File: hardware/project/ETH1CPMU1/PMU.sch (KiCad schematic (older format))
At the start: 0 parts

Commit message: Schematic design
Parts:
- added C1401: C, symbol Device:C
- added C1402: 100p, symbol Device:C
- added C1403: 1n, symbol Device:C
- added C1404: 3n3, symbol Device:C
- added C1405, C1406: 10p, symbol Device:C
- added C1407, C1409, C1411: 100n, symbol Device:C
- added C1408, C1410, C1412: 10u, symbol Device:C
- added K1401, K1402, K? (x12): HE3621A0510, symbol ETH1CPMU1:HE3621A0510
- added Q1401, Q1402: BC847, Package_TO_SOT_SMD:SOT-23, symbol Transistor_BJT:BC847
- added R1401: 5k1, symbol Device:R
- added R1402: 124k, symbol Device:R
- added R1403: 12k4, symbol Device:R
- added R1404: 1k24, symbol Device:R
- added R1405: 124, symbol Device:R
- added R1406: 12R4, symbol Device:R
- added R1407, R1408: R, symbol Device:R
- added R1410, R1411: 10k, symbol Device:R
- added U1401: AD5520, symbol ETH1CPMU1:AD5520
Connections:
- new net: K?.1, U1401.30 (GUARD)
- new net: K?.1, U1401.34 (MEASVL)
- new net: C1401.1, R1402.1, U1401.38 (MEASIOH), U1401.39 (FOH0)
- new net: R1403.1, U1401.40 (MEASI1H), U1401.41 (FOH1)
- new net: R1404.1, U1401.42 (MEASI2H), U1401.43 (FOH2)
- new net: R1405.1, U1401.44 (MEASI3H), U1401.45 (FOH3)
- new net: K1401.4, R1406.1, U1401.46 (MEASI4H)
- new net: K1402.4, R1407.1, R1408.1, U1401.47 (MEASI5H)
- new net: C1404.2, U1401.51 (COMPOUT0)
- new net: C1403.2, U1401.52 (COMPOUT1)
- new net: C1402.2, U1401.53 (COMPOUT2)
- new net: C1404.1, U1401.54 (COMPIN0)
- new net: C1403.1, U1401.55 (COMPIN1)
- new net: C1402.1, U1401.56 (COMPIN2)
- new net: K1401.1, K1402.1
- new net: K1401.3, Q1401.3 (C)
- new net: K1402.3, Q1402.3 (C)
- new net: C1406.1, Q1402.1 (B), R1411.2
- new net: C1405.1, Q1401.1 (B), R1410.2
- new net +15VF: C1411.1, C1412.1, U1401.27 (AVCC), U1401.33 (AVCCG), U1401.50 (AVCCB)
- new net +3.3VF: C1407.1, C1408.1, U1401.18 (DVDD), U1401.3 (DVDD)
- new net +5VF: K1401.2, K1402.2
- new net -15VF: C1409.1, C1410.1, U1401.26 (AVEE), U1401.29 (AVEEG), U1401.48 (AVEEB)
- new net A: K?.4
- new net AGNDF: C1409.2, C1410.2, C1411.2, C1412.2, K?.1, U1401.2 (CPL), U1401.28 (AGND), U1401.57 (REFGND), U1401.59 (REFGND), U1401.64 (CLL)
- new net B: K?.4
- new net C: K?.4
- new net DGNDF: C1405.2, C1406.2, C1407.2, C1408.2, Q1401.2 (E), Q1402.2 (E), U1401.17 (GDND), U1401.7 (DGND)
- new net E: K?.4
- new net F: K?.4, K?.4
- new net GUARDIN: K?.1, U1401.32 (GUARDIN)
- new net MEASIL: C1401.2, K?.1, R1402.2, R1403.2, R1404.2, R1405.2, R1406.2, R1407.2, R1408.2, U1401.37 (MEASIL)
- new net MEASVH: K?.1, U1401.36 (MEASHV)
- new net PMU_AC0: U1401.15 (AC0)
- new net PMU_AC1: U1401.16 (AC1)
- new net PMU_AM0: U1401.21 (AM0)
- new net PMU_AM1: U1401.20 (AM1)
- new net PMU_AM2: U1401.19 (AM2)
- new net PMU_CLHDETECT: U1401.8 (CLHDETECT)
- new net PMU_CLLDETECT: U1401.9 (CLLDETECT)
- new net PMU_CPCK: U1401.6 (CPCK)
- new net PMU_CPOH: U1401.4 (CPOH)
- new net PMU_CPOL: U1401.5 (CPOL)
- new net PMU_MSEL: U1401.24 (MSEL)
- new net PMU_QM4: R1411.1, U1401.10 (QM4)
- new net PMU_QM5: R1410.1, U1401.11 (QM5)
- new net PMU_STANDBY: U1401.22 (STANDBY)
- new net PMU_~CS: U1401.13 (~CS), U1401.25 (CPSEL)
- new net PMU_~MOE: U1401.12 (~MOE), U1401.23 (FSEL)
- new net PMU_~STB: U1401.14 (~STB)

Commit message: Schematic design
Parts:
- removed K? (x12): HE3621A0510, symbol ETH1CPMU1:HE3621A0510
- added C1303, C1304, C1305: 100n, symbol Device:C
- added C1413, C1414, C1415, C1416, C1417, C1418: 10p, symbol Device:C
- added K1403, K1404, K1405, K1406, K1407, K1408: HE3621A0510, symbol ETH1CPMU1:HE3621A0510
- added Q1403, Q1404, Q1405, Q1406, Q1407, Q1408: BC847, Package_TO_SOT_SMD:SOT-23, symbol Transistor_BJT:BC847
- added R1409: 5k1, symbol Device:R
- added R1412, R1413, R1414, R1415, R1416, R1417: 10k, symbol Device:R
- added U1402: AD8010, symbol ETH1CPMU1:AD8010
- added U1403: DG419LEUA, Package_SO:MSOP-8_3x3mm_P0.65mm, symbol Analog_Switch:DG419LEUA
- R1402: value 124k -> 125k
- R1403: value 12k4 -> 12k5
- R1404: value 1k24 -> 1k25
- R1405: value 124 -> 125
- R1406: value 12R4 -> 12R5
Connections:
- net +15VF: now also C1304.1, U1402.7 (V+), U1403.4 (V+)
- net +3.3VF: now also C1303.1, U1403.5 (VL)
- net +5VF: now also K1403.2, K1404.2, K1405.2, K1406.2, K1407.2, K1408.2
- net -15VF: now also C1305.1, U1402.4 (V-), U1403.7 (V-)
- net A: now also K1404.4
- net AGNDF: now also K1408.1
- net B: now also K1405.4
- net C: now also K1407.4
- net DGNDF: now also C1303.2, C1304.2, C1305.2, C1413.2, C1414.2, C1415.2, C1416.2, C1417.2, C1418.2, Q1403.2 (E), Q1404.2 (E), Q1405.2 (E), Q1406.2 (E), Q1407.2 (E), Q1408.2 (E), U1403.3 (GND)
- net E: now also K1408.4
- net F: now also K1403.4, K1406.4
- net PMU_QM4: now also R1410.1; no longer R1411.1
- net PMU_QM5: now also R1411.1; no longer R1410.1
- net PMU_~CS: no longer U1401.25 (CPSEL)
- net at U1401.30 (GUARD): now also K1407.1
- net at U1401.34 (MEASVL): now also K1405.1
- net at U1401.49 (FOH): now also R1401.2
- net PMU_MEASOUT: now reaches U1401.58 (MEASOUT)
- net PMU_MEASIOUT: now reaches U1401.60 (MEASIOUT)
- net PMU_MEASVOUT: now reaches U1401.61 (MEASVOUT)
- net at U1401.62 (FIN): now also U1403.1
- net at K1401.1, K1402.1: now also R1409.1, U1402.6
- net at R1401.1: now also U1402.3 (+)
- net GUARDIN: no longer names the net of U1401.32 (GUARDIN)
- net GUARDIN: now also K1406.1
- net MEASIL: no longer names the net of C1401.2, R1402.2, R1403.2, R1404.2, R1405.2, R1406.2, R1407.2, R1408.2, U1401.37 (MEASIL)
- net MEASIL: now also K1403.1
- net MEASVH: no longer names the net of U1401.36 (MEASHV)
- net MEASVH: now also K1404.1
- new net: C1413.1, Q1403.1 (B), R1412.2
- new net: K1403.3, Q1403.3 (C)
- new net: C1414.1, Q1404.1 (B), R1413.2
- new net: K1404.3, Q1404.3 (C)
- new net: K1405.3, Q1405.3 (C)
- new net: K1406.3, Q1406.3 (C)
- new net: K1407.3, Q1407.3 (C)
- new net: K1408.3, Q1408.3 (C)
- new net: C1415.1, Q1405.1 (B), R1414.2
- new net: R1409.2, U1402.2 (-)
- new net: C1416.1, Q1406.1 (B), R1415.2
- new net: C1417.1, Q1407.1 (B), R1416.2
- new net: C1418.1, Q1408.1 (B), R1417.2
- new net AC_FOURCE: U1403.8
- new net DC_FOURCE: U1403.2
- new net FOURCE_SELECT: U1403.6
- new net PMU_CPSEL: U1401.25 (CPSEL)
- new net R_GND: R1417.1
- new net R_GUARD: R1416.1
- new net R_GUARDIN: R1415.1
- new net R_MEASHV: R1413.1
- new net R_MEASIL: R1412.1
- new net R_MEASVL: R1414.1
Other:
- note added: "RELAY CONTROL"
- moved on the sheet: C1401, C1402, C1403, C1404, C1405, C1406, C1407, C1408, C1409, C1410, C1411, C1412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

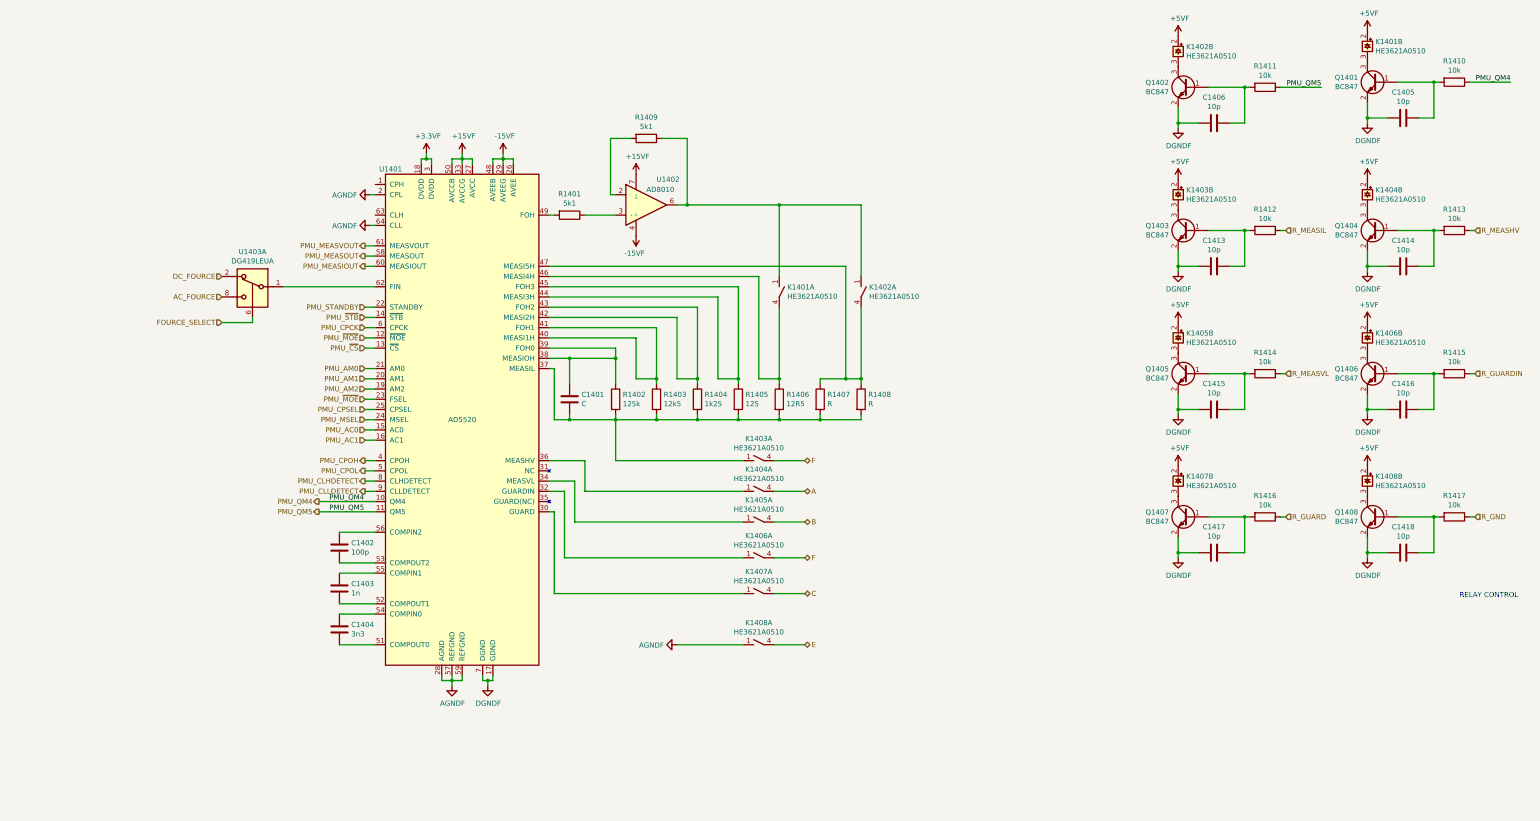
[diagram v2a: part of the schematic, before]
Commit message: Function generator schematic design.
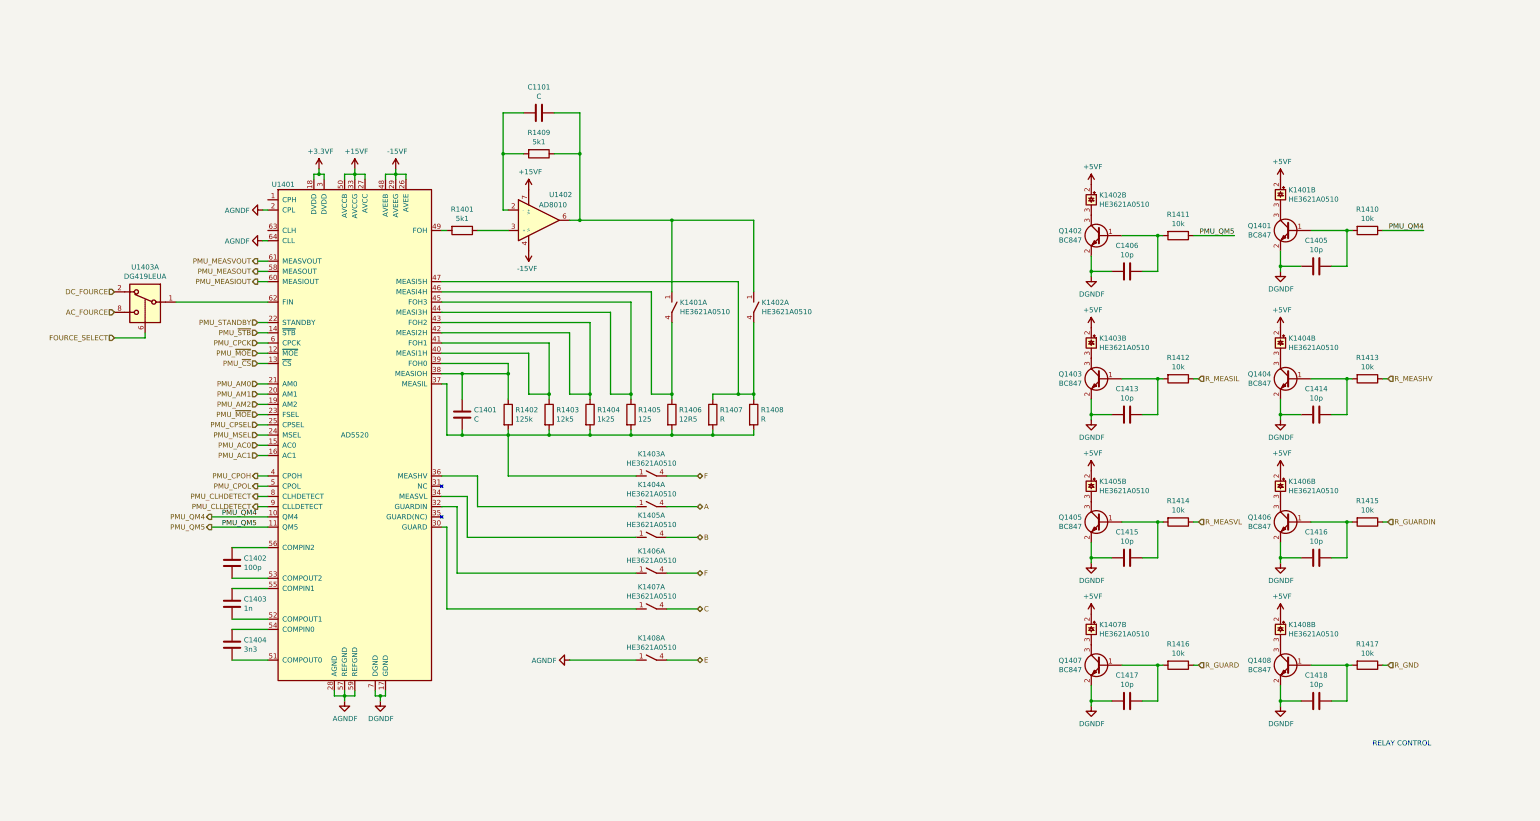
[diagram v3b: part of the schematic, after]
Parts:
- added C1101: C, symbol Device:C
- C1303, C1304, C1305, C1402, C1403, C1404, C1405, C1406, C1407, C1409, C1411, C1413, C1414, C1415, C1416, C1417, C1418: footprint (none) -> Capacitor_SMD:C_0603_1608Metric_Pad1.05x0.95mm_HandSolder
- C1408, C1410, C1412: footprint (none) -> Capacitor_SMD:C_1206_3216Metric_Pad1.42x1.75mm_HandSolder
- R1410, R1411, R1412, R1413, R1414, R1415, R1416, R1417: footprint (none) -> Resistor_SMD:R_0603_1608Metric_Pad1.05x0.95mm_HandSolder
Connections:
- net at R1409.2, U1402.2 (-): now also C1101.2
- net at K1401.1, K1402.1, R1409.1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: now also C1101.1
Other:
- moved on the sheet: C1401, C1402, C1403, C1404, C1405, C1406, C1413, C1414, C1415, C1416, C1417, C1418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

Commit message: Function generator schematic development.
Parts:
- C1101, C1401: footprint (none) -> Capacitor_SMD:C_0603_1608Metric_Pad1.05x0.95mm_HandSolder
- R1401, R1402, R1403, R1404, R1405, R1406, R1409: footprint (none) -> Resistor_SMD:R_0603_1608Metric_Pad1.05x0.95mm_HandSolder
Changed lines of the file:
@@
 EESchema Schematic File Version 4
-LIBS:ETH1CPMU1-cache
 EELAYER 30 0
 EELAYER END
@@
 F 0 "C1401" H 5315 4496 50  0000 L CNN
 F 1 "C" H 5315 4405 50  0000 L CNN
-F 2 "" H 5238 4300 50  0001 C CNN
+F 2 "Capacitor_SMD:C_0603_1608Metric_Pad1.05x0.95mm_HandSolder" H 5238 4300 50  0001 C CNN
 F 3 "~" H 5200 4450 50  0001 C CNN
 	1    5200 4450
@@
 F 0 "R1401" V 4993 2650 50  0000 C CNN
 F 1 "5k1" V 5084 2650 50  0000 C CNN
-F 2 "" V 5130 2650 50  0001 C CNN
+F 2 "Resistor_SMD:R_0603_1608Metric_Pad1.05x0.95mm_HandSolder" V 5130 2650 50  0001 C CNN
 F 3 "~" H 5200 2650 50  0001 C CNN
 	1    5200 2650
@@
 F 0 "R1405" H 6920 4496 50  0000 L CNN
 F 1 "125" H 6920 4405 50  0000 L CNN
-F 2 "" V 6780 4450 50  0001 C CNN
+F 2 "Resistor_SMD:R_0603_1608Metric_Pad1.05x0.95mm_HandSolder" V 6780 4450 50  0001 C CNN
 F 3 "~" H 6850 4450 50  0001 C CNN
 	1    6850 4450
@@
 F 0 "R1404" H 6520 4496 50  0000 L CNN
 F 1 "1k25" H 6520 4405 50  0000 L CNN
-F 2 "" V 6380 4450 50  0001 C CNN
+F 2 "Resistor_SMD:R_0603_1608Metric_Pad1.05x0.95mm_HandSolder" V 6380 4450 50  0001 C CNN
 F 3 "~" H 6450 4450 50  0001 C CNN
 	1    6450 4450
@@
 F 0 "R1403" H 6120 4496 50  0000 L CNN
 F 1 "12k5" H 6120 4405 50  0000 L CNN
-F 2 "" V 5980 4450 50  0001 C CNN
+F 2 "Resistor_SMD:R_0603_1608Metric_Pad1.05x0.95mm_HandSolder" V 5980 4450 50  0001 C CNN
 F 3 "~" H 6050 4450 50  0001 C CNN
 	1    6050 4450
@@
 F 0 "R1402" H 5720 4496 50  0000 L CNN
 F 1 "125k" H 5720 4405 50  0000 L CNN
-F 2 "" V 5580 4450 50  0001 C CNN
+F 2 "Resistor_SMD:R_0603_1608Metric_Pad1.05x0.95mm_HandSolder" V 5580 4450 50  0001 C CNN
 F 3 "~" H 5650 4450 50  0001 C CNN
 	1    5650 4450
@@
 F 0 "R1406" H 7320 4496 50  0000 L CNN
 F 1 "12R5" H 7320 4405 50  0000 L CNN
-F 2 "" V 7180 4450 50  0001 C CNN
+F 2 "Resistor_SMD:R_0603_1608Metric_Pad1.05x0.95mm_HandSolder" V 7180 4450 50  0001 C CNN
 F 3 "~" H 7250 4450 50  0001 C CNN
 	1    7250 4450
@@
 F 0 "R1409" V 5743 1900 50  0000 C CNN
 F 1 "5k1" V 5834 1900 50  0000 C CNN
-F 2 "" V 5880 1900 50  0001 C CNN
+F 2 "Resistor_SMD:R_0603_1608Metric_Pad1.05x0.95mm_HandSolder" V 5880 1900 50  0001 C CNN
 F 3 "~" H 5950 1900 50  0001 C CNN
 	1    5950 1900
@@
 F 0 "C1101" V 5698 1500 50  0000 C CNN
 F 1 "C" V 5789 1500 50  0000 C CNN
-F 2 "" H 5988 1350 50  0001 C CNN
+F 2 "Capacitor_SMD:C_0603_1608Metric_Pad1.05x0.95mm_HandSolder" H 5988 1350 50  0001 C CNN
 F 3 "~" H 5950 1500 50  0001 C CNN
 	1    5950 1500
